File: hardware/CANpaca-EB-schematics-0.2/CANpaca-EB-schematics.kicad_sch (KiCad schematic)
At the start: 132 parts, among them J11 Conn_01x03_Male, J12 A2501WV-4P, J13 A2501WV-3P, J14 A2501WV-5P, J16 A2501WV-3P, J17 A2501WV-2P, J2 FAN_0, J4 Conn_01x03_Male, J5 FAN_1, J6 Screw_Terminal_01x02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

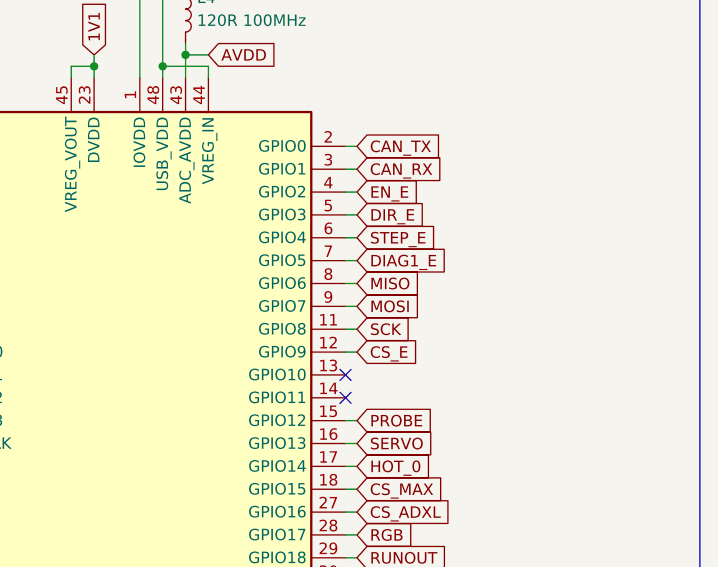
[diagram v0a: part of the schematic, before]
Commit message: changed to hardware spi
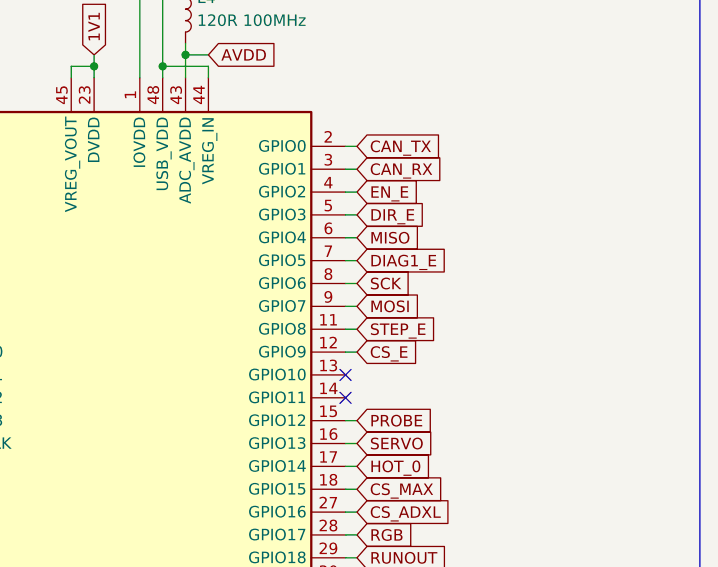
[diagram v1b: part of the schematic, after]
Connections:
- net MISO: now also U10.6 (GPIO4); no longer U10.8 (GPIO6)
- net SCK: now also U10.8 (GPIO6); no longer U10.11 (GPIO8)
- net STEP_E: now also U10.11 (GPIO8); no longer U10.6 (GPIO4)
